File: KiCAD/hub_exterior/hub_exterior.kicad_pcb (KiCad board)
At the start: 2 copper layers, 50 x 50 mm, 21 parts, among them Q1 BC337, X2 LLUVIA, X4 GPS, X5 LED_ROJO, X6 BUZZER

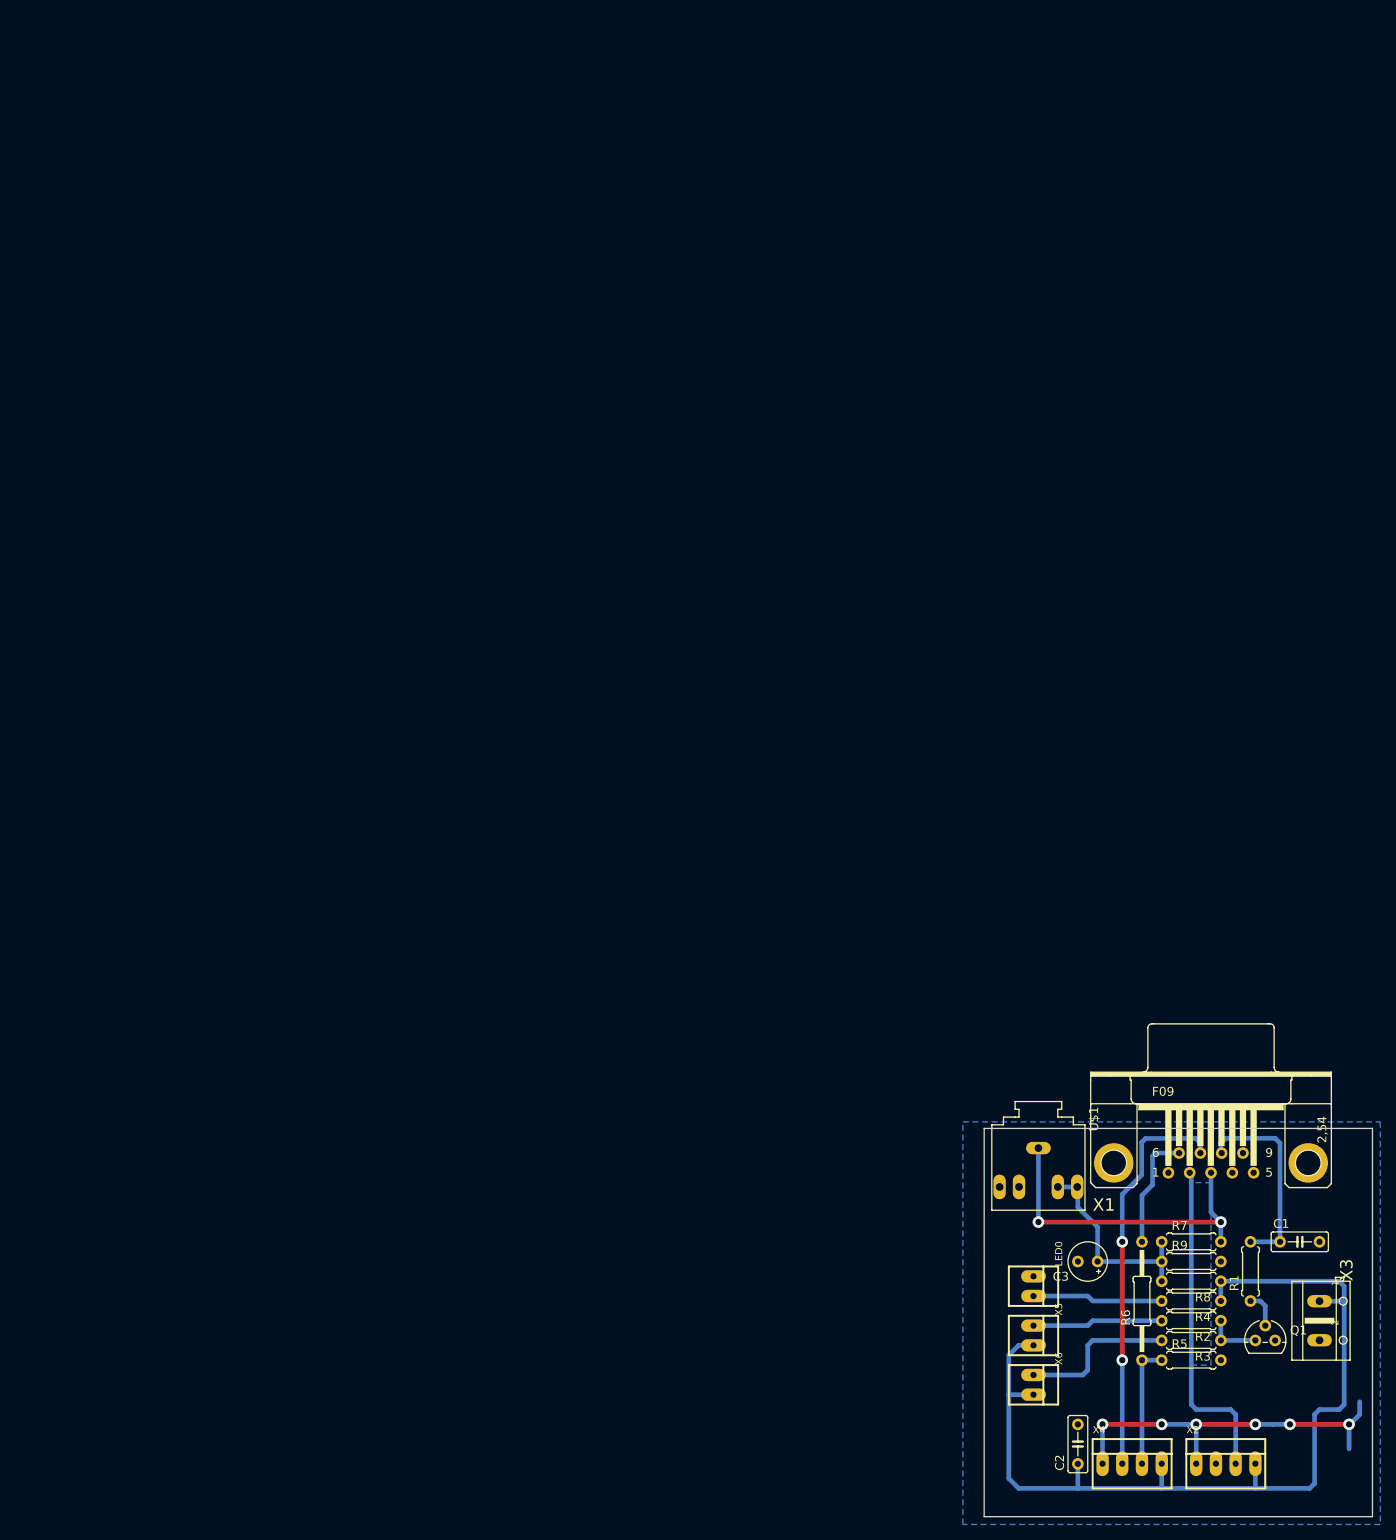
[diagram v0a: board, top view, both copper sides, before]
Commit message: rediseño hub exterior
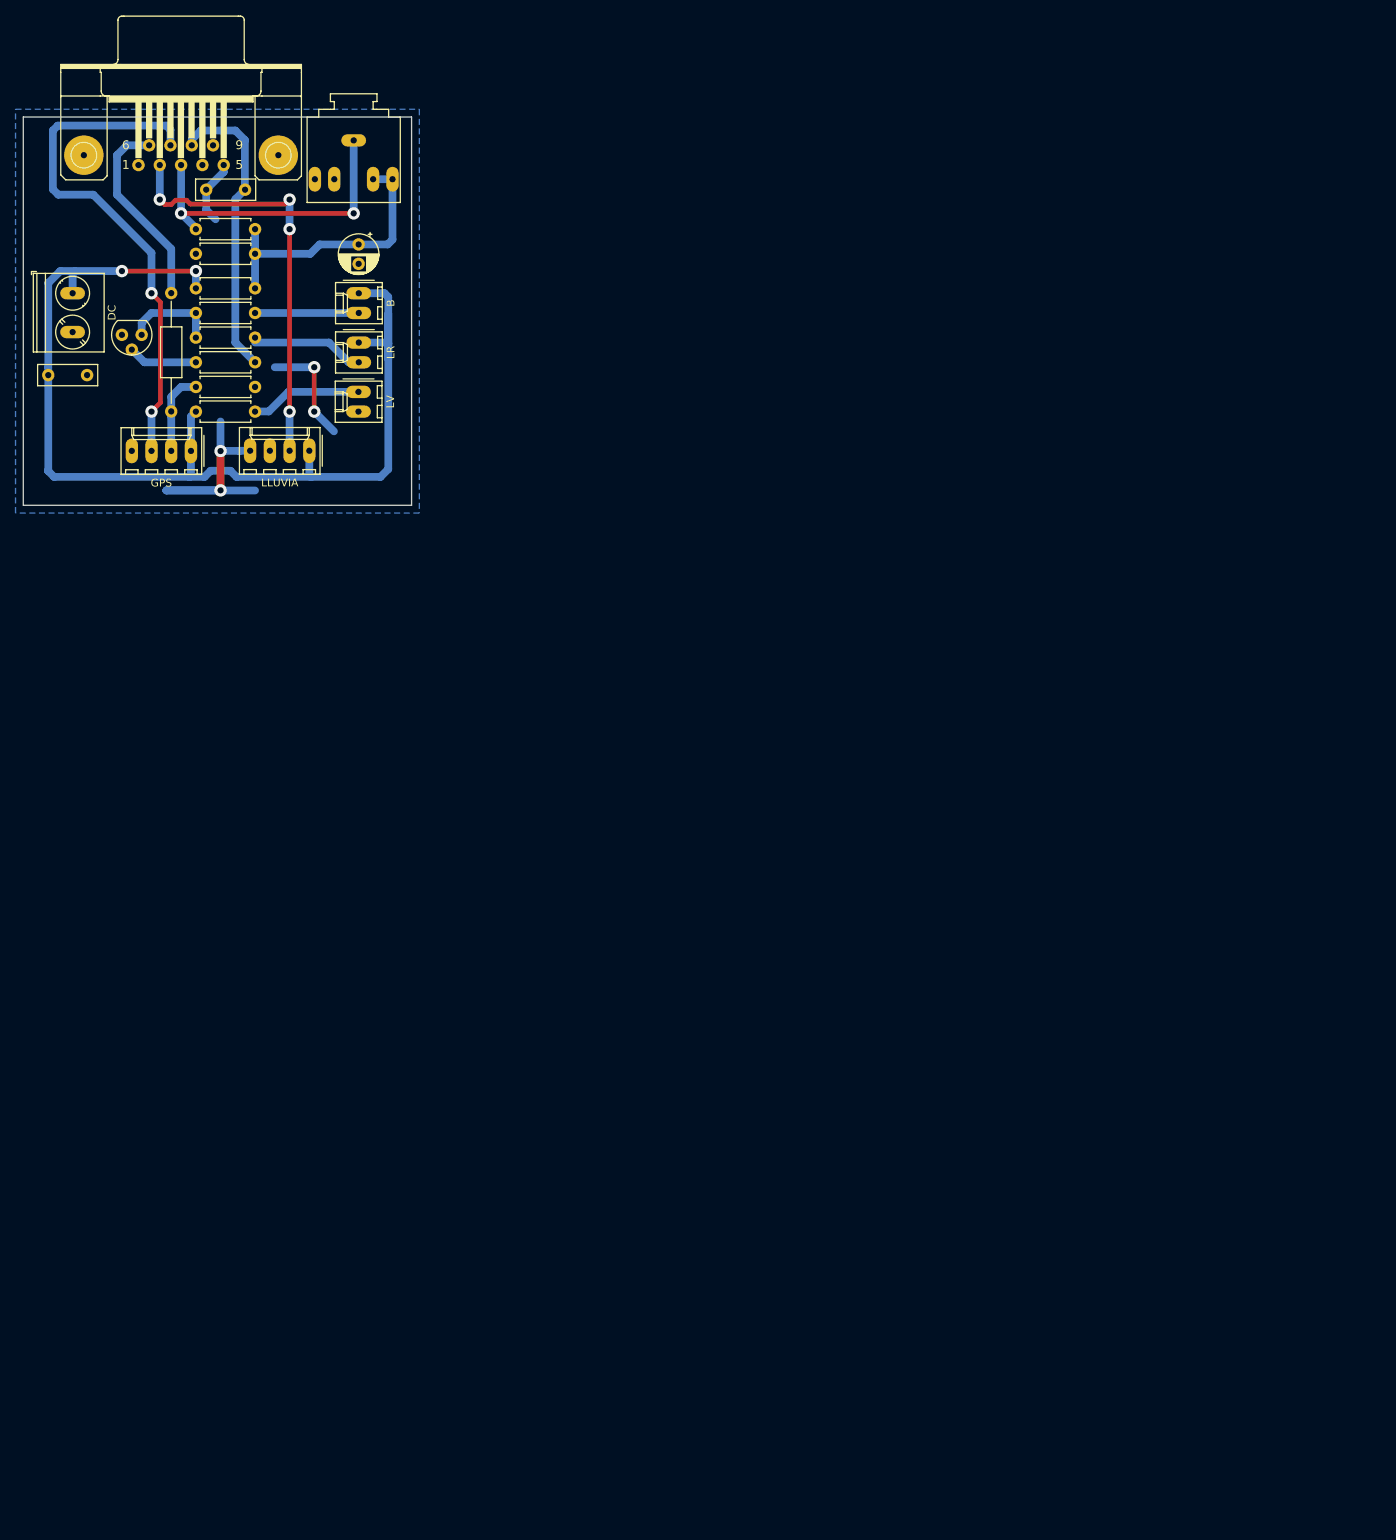
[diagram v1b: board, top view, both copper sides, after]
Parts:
- removed LED0: LED_VERDE, hub_exterior:22-23-2021
- removed X2: LLUVIA, hub_exterior:22-23-2041
- removed X3: , hub_exterior:AK500_2
- removed X4: GPS, hub_exterior:22-23-2041
- removed X5: LED_ROJO, hub_exterior:22-23-2021
- removed X6: BUZZER, hub_exterior:22-23-2021
- added B: BUZZER, Connector_Molex:Molex_KK-254_AE-6410-02A_1x02_P2.54mm_Vertical, F.Cu at (43.2, -27.3)
- added DC: AK500/2, TerminalBlock_Phoenix:TerminalBlock_Phoenix_PT-1,5-2-5.0-H_1x02_P5.00mm_Horizontal, F.Cu at (6.35, -27.3)
- added GPS: GPS, Connector_Molex:Molex_KK-254_AE-6410-04A_1x04_P2.54mm_Vertical, F.Cu at (21.6, -7.00)
- added LLUVIA: LLUVIA, Connector_Molex:Molex_KK-254_AE-6410-04A_1x04_P2.54mm_Vertical, F.Cu at (36.8, -7.03)
- added LR: LED_ROJO, Connector_Molex:Molex_KK-254_AE-6410-02A_1x02_P2.54mm_Vertical, F.Cu at (43.2, -21.0)
- added LV: LED_VERDE, Connector_Molex:Molex_KK-254_AE-6410-02A_1x02_P2.54mm_Vertical, F.Cu at (43.2, -14.6)
- C1, C2: footprint hub_exterior:C050-025X075 -> Capacitor_THT:C_Disc_D7.5mm_W2.5mm_P5.00mm
- C3: footprint hub_exterior:E2,5-5 -> Capacitor_THT:CP_Radial_D5.0mm_P2.50mm
- Q1: footprint hub_exterior:TO92 -> Package_TO_SOT_THT:TO-92
- R1, R2, R3, R4, R5, R7, R8, R9: footprint hub_exterior:0207_7 -> Resistor_THT:R_Axial_DIN0207_L6.3mm_D2.5mm_P7.62mm_Horizontal
- R6: footprint hub_exterior:0207_15 -> Resistor_THT:R_Axial_DIN0207_L6.3mm_D2.5mm_P15.24mm_Horizontal
- X1: value (none) -> F09HP
- moved Q1 194.2 mm to (15.2, -21.9), turned to 180 degrees
- moved C1 191.8 mm to (28.6, -40.6), turned to 180 degrees
- moved C2 191.1 mm to (3.21, -16.8), turned to 0 degrees
- moved X1 185.6 mm to (20.3, -45.1)
- moved R3 184.2 mm to (22.2, -24.8), turned to 0 degrees
- moved R8 181.1 mm to (22.2, -27.9), turned to 0 degrees
- moved R2 180.2 mm to (22.2, -21.6), turned to 0 degrees
- moved R1 179.3 mm to (22.2, -18.4), turned to 0 degrees
- moved R5 179.3 mm to (22.2, -15.2)
- moved R7 177.6 mm to (29.8, -35.6), turned to 180 degrees
- moved R9 177.1 mm to (29.8, -32.4), turned to 180 degrees
- moved R4 171.9 mm to (22.2, -12.1), turned to 0 degrees
- moved R6 169.6 mm to (19.1, -12.1)
- moved C3 161.2 mm to (43.2, -33.6), turned to -90 degrees
- moved U$1 156.9 mm to (42.5, -47.0)
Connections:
- net N$4 renamed /N$4
- net N$8 renamed /N$8
- R7 pad 1: N$14 -> Net-(C3-Pad+)
- R8 pad 2: N$14 -> Net-(C3-Pad+)
- R9 pad 1: N$14 -> Net-(C3-Pad+)
- U$1 pad P$4: (no net) -> unconnected-(U$1-PadP$4)
- U$1 pad P$5: N$14 -> Net-(C3-Pad+)
- U$1 pad P$6: (no net) -> unconnected-(U$1-PadP$6)
- U$1 pad P$7: N$14 -> Net-(C3-Pad+)
- X1 pad 1: (no net) -> unconnected-(X1-Pad1)
- X1 pad 4: (no net) -> unconnected-(X1-Pad4)
- X1 pad 9: (no net) -> unconnected-(X1-Pad9)
- X1 pad G1: GND -> unconnected-(X1-PadG1)
- X1 pad G2: GND -> unconnected-(X1-PadG2)
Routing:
- net Net-(C3-Pad+): track 0.00 -> 37.0 mm
- net N$14: track 26.6 -> 0.00 mm
- net +5V: track 122.7 -> 142.4 mm, vias 0 -> 2
- net Net-(X1-Pad7): track 51.7 -> 67.7 mm
- net /N$8: track 26.0 -> 38.1 mm
- net Net-(X1-Pad2): track 42.6 -> 54.4 mm, vias 0 -> 4
- net Net-(R6-Pad2): track 15.2 -> 25.3 mm
- net Net-(R3-Pad2): track 20.2 -> 13.4 mm
- net GND: track 48.6 -> 53.9 mm, vias 6 -> 4
- net Net-(Q1-Pad3): track 6.98 -> 12.2 mm
- net Net-(R5-Pad1): track 15.9 -> 11.3 mm
- net Net-(Q1-Pad2): track 4.71 -> 8.93 mm
- net Net-(LED0-Pad2): track 16.8 -> 14.4 mm
- net Net-(R2-Pad2): track 16.8 -> 14.4 mm
- net /N$4: track 42.4 -> 40.3 mm
- removed copper zone on B.Cu, net (none)

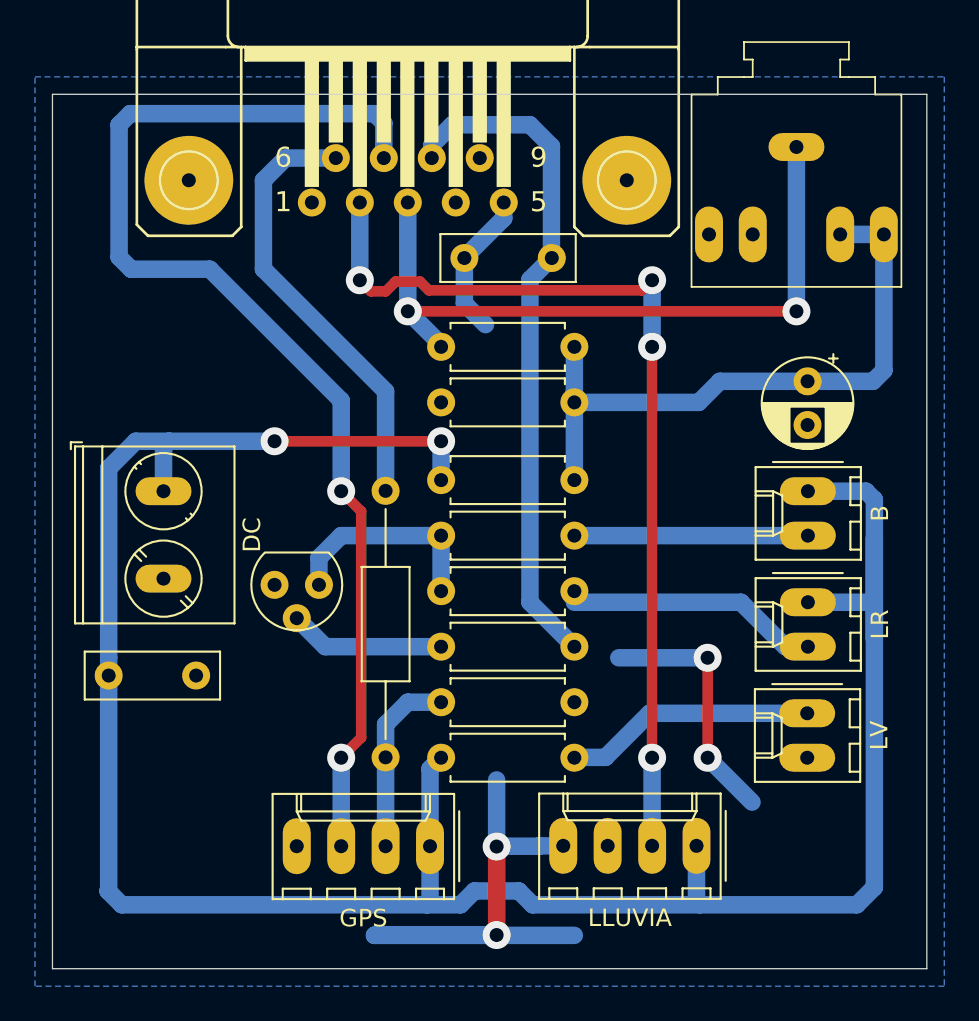
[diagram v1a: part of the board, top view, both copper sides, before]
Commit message: engrosado pads hub exterior
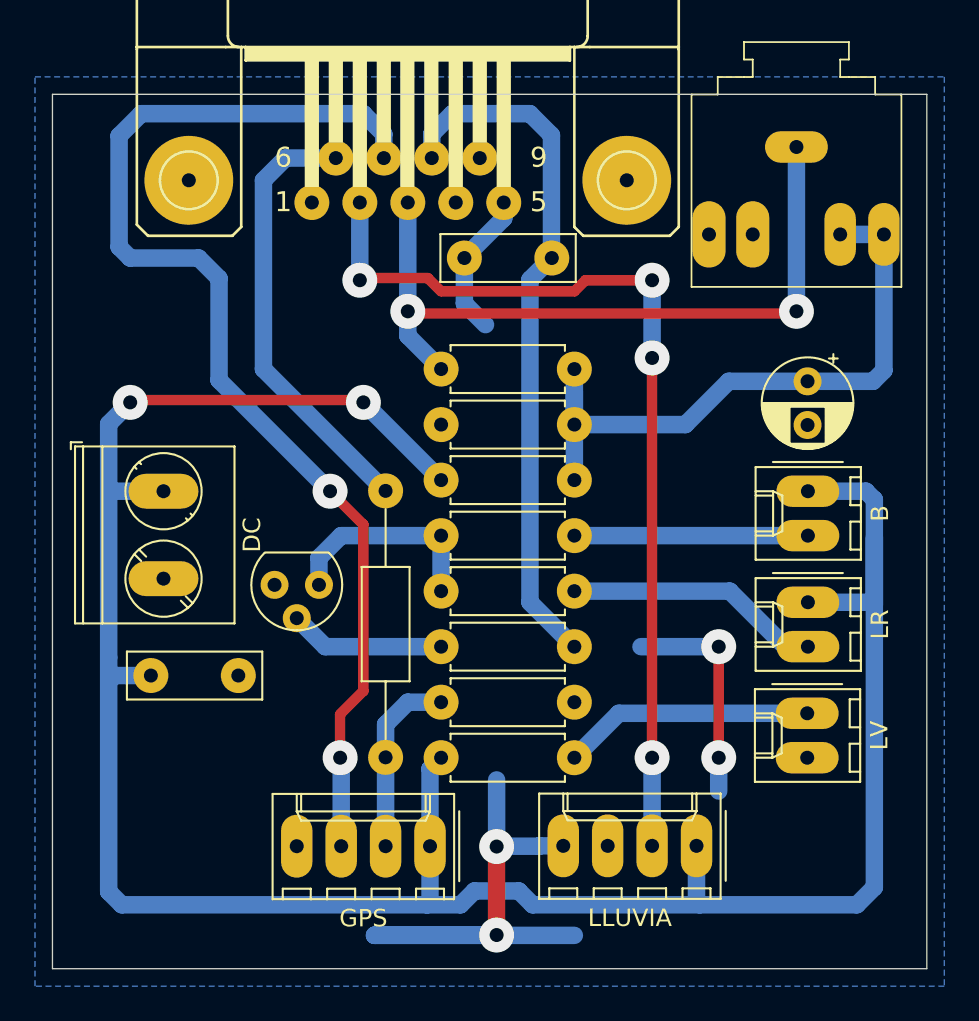
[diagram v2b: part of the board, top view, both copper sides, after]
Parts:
- moved C2 2.41 mm to (5.63, -16.8)
- moved R7 1.27 mm to (29.8, -34.3)
- moved R9 1.27 mm to (29.8, -31.1)
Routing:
- net +5V: track 142.4 -> 145.2 mm
- net GND: track 53.9 -> 52.2 mm
- net /N$4: track 40.3 -> 41.7 mm
- net /N$8: track 38.1 -> 39.4 mm
- net Net-(X1-Pad7): track 67.7 -> 66.8 mm
- net Net-(C3-Pad+): track 37.0 -> 37.5 mm
